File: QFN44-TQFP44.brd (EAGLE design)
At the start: 21.6 x 57.1 mm, 9 parts

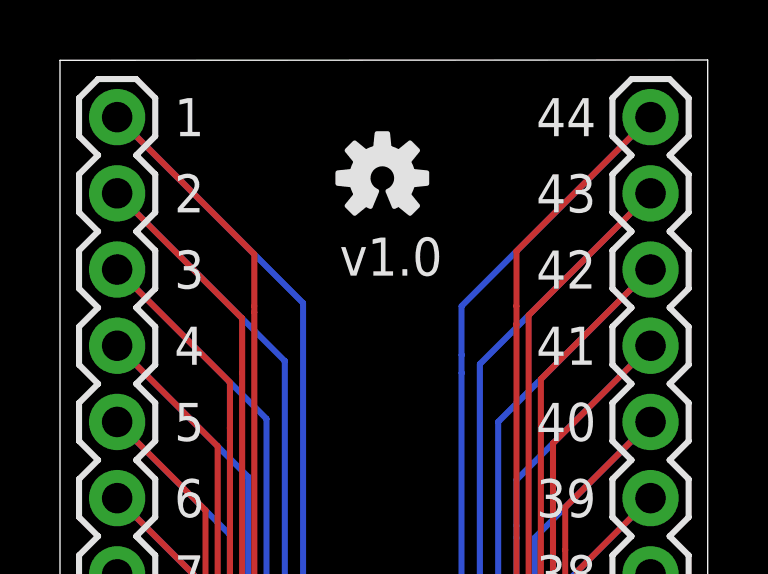
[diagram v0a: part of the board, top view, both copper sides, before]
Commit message: Silk and board revision
Worked several silk screen issues and narrowed some boards.
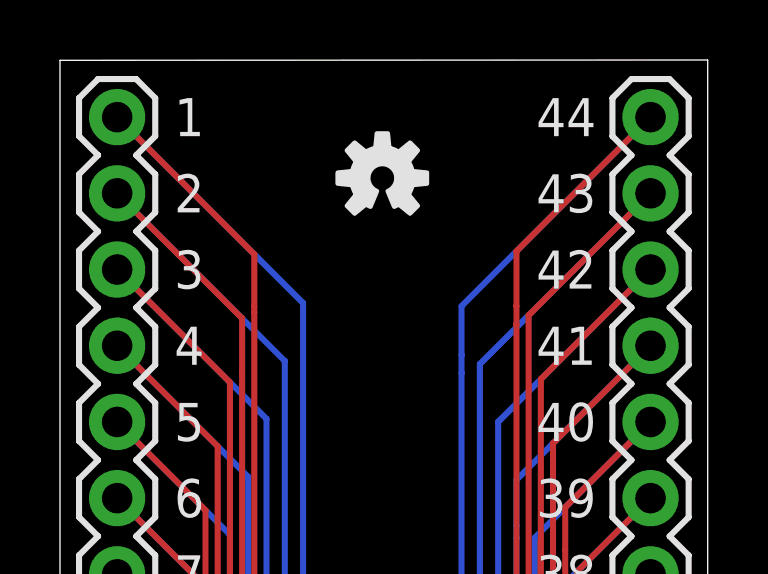
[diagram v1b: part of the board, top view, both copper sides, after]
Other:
- board text removed: "v1.0"
